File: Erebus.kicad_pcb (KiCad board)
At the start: 2 copper layers, 7 parts, among them U1 STM32F303CBTx, U2 74HC4067, U3 74HC4067, U4 74HC4067, U5 74HC4067, U6 74HC4067, U7 74HC4067

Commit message: Added All the Keyswitches Required
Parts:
- added C1: 100n, Capacitor_SMD:C_0402_1005Metric, F.Cu at (-203.2, 256.6)
- added C10: 100n, Capacitor_SMD:C_0402_1005Metric, F.Cu at (-153.1, 282.8)
- added C100: 100n, Capacitor_SMD:C_0402_1005Metric, F.Cu at (-128.1, 282.8)
- added C101: 100n, Capacitor_SMD:C_0402_1005Metric, F.Cu at (-27.9, 280.8)
- added C102: 100n, Capacitor_SMD:C_0402_1005Metric, F.Cu at (-27.9, 282.8)
- added C103: 100n, Capacitor_SMD:C_0402_1005Metric, F.Cu at (-178.2, 280.8)
- added C104: 100n, Capacitor_SMD:C_0402_1005Metric, F.Cu at (-178.2, 282.8)
- added C105: 100n, Capacitor_SMD:C_0402_1005Metric, F.Cu at (-143.1, 192.1)
- added C106: 100n, Capacitor_SMD:C_0402_1005Metric, F.Cu at (-143.1, 194.1)
- added C107: 100n, Capacitor_SMD:C_0402_1005Metric, F.Cu at (-178.2, 256.6)
- added C108: 100n, Capacitor_SMD:C_0402_1005Metric, F.Cu at (-178.2, 258.6)
- added C109: 100n, Capacitor_SMD:C_0402_1005Metric, F.Cu at (-42.9, 216.3)
- added C11: 100n, Capacitor_SMD:C_0402_1005Metric, F.Cu at (-143.1, 216.3)
- added C110: 100n, Capacitor_SMD:C_0402_1005Metric, F.Cu at (-42.9, 218.3)
- added C111: 100n, Capacitor_SMD:C_0402_1005Metric, F.Cu at (-78.0, 280.8)
- added C112: 100n, Capacitor_SMD:C_0402_1005Metric, F.Cu at (-78.0, 282.8)
- added C113: 100n, Capacitor_SMD:C_0402_1005Metric, F.Cu at (-178.2, 329.1)
- added C114: 100n, Capacitor_SMD:C_0402_1005Metric, F.Cu at (-178.2, 331.1)
- added C115: 100n, Capacitor_SMD:C_0402_1005Metric, F.Cu at (-53.0, 377.4)
- added C116: 100n, Capacitor_SMD:C_0402_1005Metric, F.Cu at (-53.0, 379.4)
- added C117: 100n, Capacitor_SMD:C_0402_1005Metric, F.Cu at (-118.0, 192.1)
- added C118: 100n, Capacitor_SMD:C_0402_1005Metric, F.Cu at (-118.0, 194.1)
- added C119: 100n, Capacitor_SMD:C_0402_1005Metric, F.Cu at (-53.0, 304.9)
- added C12: 100n, Capacitor_SMD:C_0402_1005Metric, F.Cu at (-143.1, 218.3)
- added C120: 100n, Capacitor_SMD:C_0402_1005Metric, F.Cu at (-53.0, 306.9)
- added C121: 100n, Capacitor_SMD:C_0402_1005Metric, F.Cu at (-2.90, 401.6)
- added C122: 100n, Capacitor_SMD:C_0402_1005Metric, F.Cu at (-2.90, 403.6)
- added C123: 100n, Capacitor_SMD:C_0402_1005Metric, F.Cu at (-103.1, 329.1)
- added C124: 100n, Capacitor_SMD:C_0402_1005Metric, F.Cu at (-103.1, 331.1)
- added C125: 100n, Capacitor_SMD:C_0402_1005Metric, F.Cu at (-228.3, 377.4)
- added C126: 100n, Capacitor_SMD:C_0402_1005Metric, F.Cu at (-228.3, 379.4)
- added C127: 100n, Capacitor_SMD:C_0402_1005Metric, F.Cu at (-27.9, 377.4)
- added C128: 100n, Capacitor_SMD:C_0402_1005Metric, F.Cu at (-27.9, 379.4)
- added C129: 100n, Capacitor_SMD:C_0402_1005Metric, F.Cu at (-128.1, 256.6)
- added C13: 100n, Capacitor_SMD:C_0402_1005Metric, F.Cu at (-103.1, 377.4)
- added C130: 100n, Capacitor_SMD:C_0402_1005Metric, F.Cu at (-128.1, 258.6)
- added C131: 100n, Capacitor_SMD:C_0402_1005Metric, F.Cu at (-153.1, 329.1)
- added C132: 100n, Capacitor_SMD:C_0402_1005Metric, F.Cu at (-153.1, 331.1)
- added C133: 100n, Capacitor_SMD:C_0402_1005Metric, F.Cu at (-203.2, 280.8)
- added C134: 100n, Capacitor_SMD:C_0402_1005Metric, F.Cu at (-203.2, 282.8)
- added C135: 100n, Capacitor_SMD:C_0402_1005Metric, F.Cu at (-128.1, 304.9)
- added C136: 100n, Capacitor_SMD:C_0402_1005Metric, F.Cu at (-128.1, 306.9)
- added C137: 100n, Capacitor_SMD:C_0402_1005Metric, F.Cu at (-228.3, 353.3)
- added C138: 100n, Capacitor_SMD:C_0402_1005Metric, F.Cu at (-228.3, 355.2)
- added C139: 100n, Capacitor_SMD:C_0402_1005Metric, F.Cu at (-27.9, 329.1)
- added C14: 100n, Capacitor_SMD:C_0402_1005Metric, F.Cu at (-103.1, 379.4)
- added C140: 100n, Capacitor_SMD:C_0402_1005Metric, F.Cu at (-27.9, 331.1)
- added C141: 100n, Capacitor_SMD:C_0402_1005Metric, F.Cu at (-2.90, 256.6)
- added C142: 100n, Capacitor_SMD:C_0402_1005Metric, F.Cu at (-2.90, 258.6)
- added C143: 100n, Capacitor_SMD:C_0402_1005Metric, F.Cu at (-203.2, 353.3)
- added C144: 100n, Capacitor_SMD:C_0402_1005Metric, F.Cu at (-203.2, 355.2)
- added C145: 100n, Capacitor_SMD:C_0402_1005Metric, F.Cu at (-17.9, 192.1)
- added C146: 100n, Capacitor_SMD:C_0402_1005Metric, F.Cu at (-17.9, 194.1)
- added C147: 100n, Capacitor_SMD:C_0402_1005Metric, F.Cu at (-228.3, 280.8)
- added C148: 100n, Capacitor_SMD:C_0402_1005Metric, F.Cu at (-228.3, 282.8)
- added C149: 100n, Capacitor_SMD:C_0402_1005Metric, F.Cu at (-178.2, 377.4)
- added C15: 100n, Capacitor_SMD:C_0402_1005Metric, F.Cu at (-27.9, 304.9)
- added C150: 100n, Capacitor_SMD:C_0402_1005Metric, F.Cu at (-178.2, 379.4)
- added C151: 100n, Capacitor_SMD:C_0402_1005Metric, F.Cu at (-203.2, 377.4)
- added C152: 100n, Capacitor_SMD:C_0402_1005Metric, F.Cu at (-203.2, 379.4)
- added C153: 100n, Capacitor_SMD:C_0402_1005Metric, F.Cu at (-53.0, 280.8)
- added C154: 100n, Capacitor_SMD:C_0402_1005Metric, F.Cu at (-53.0, 282.8)
- added C155: 100n, Capacitor_SMD:C_0402_1005Metric, F.Cu at (-93.0, 216.3)
- added C156: 100n, Capacitor_SMD:C_0402_1005Metric, F.Cu at (-93.0, 218.3)
- added C157: 100n, Capacitor_SMD:C_0402_1005Metric, F.Cu at (-103.1, 304.9)
- added C158: 100n, Capacitor_SMD:C_0402_1005Metric, F.Cu at (-103.1, 306.9)
- added C159: 100n, Capacitor_SMD:C_0402_1005Metric, F.Cu at (-78.0, 329.1)
- added C16: 100n, Capacitor_SMD:C_0402_1005Metric, F.Cu at (-27.9, 306.9)
- added C160: 100n, Capacitor_SMD:C_0402_1005Metric, F.Cu at (-78.0, 331.1)
- added C161: 100n, Capacitor_SMD:C_0402_1005Metric, F.Cu at (-153.1, 304.9)
- added C162: 100n, Capacitor_SMD:C_0402_1005Metric, F.Cu at (-153.1, 306.9)
- added C163: 100n, Capacitor_SMD:C_0402_1005Metric, F.Cu at (-128.1, 401.6)
- added C164: 100n, Capacitor_SMD:C_0402_1005Metric, F.Cu at (-128.1, 403.6)
- added C17: 100n, Capacitor_SMD:C_0402_1005Metric, F.Cu at (-153.1, 401.6)
- added C18: 100n, Capacitor_SMD:C_0402_1005Metric, F.Cu at (-153.1, 403.6)
- added C19: 100n, Capacitor_SMD:C_0402_1005Metric, F.Cu at (-203.2, 304.9)
- added C2: 100n, Capacitor_SMD:C_0402_1005Metric, F.Cu at (-203.2, 258.6)
- added C20: 100n, Capacitor_SMD:C_0402_1005Metric, F.Cu at (-203.2, 306.9)
- added C21: 100n, Capacitor_SMD:C_0402_1005Metric, F.Cu at (-153.1, 353.3)
- added C22: 100n, Capacitor_SMD:C_0402_1005Metric, F.Cu at (-153.1, 355.2)
- added C23: 100n, Capacitor_SMD:C_0402_1005Metric, F.Cu at (-78.0, 353.3)
- added C24: 100n, Capacitor_SMD:C_0402_1005Metric, F.Cu at (-78.0, 355.2)
- added C25: 100n, Capacitor_SMD:C_0402_1005Metric, F.Cu at (-42.9, 192.1)
- added C26: 100n, Capacitor_SMD:C_0402_1005Metric, F.Cu at (-42.9, 194.1)
- added C27: 100n, Capacitor_SMD:C_0402_1005Metric, F.Cu at (-78.0, 401.6)
- added C28: 100n, Capacitor_SMD:C_0402_1005Metric, F.Cu at (-78.0, 403.6)
- added C29: 100n, Capacitor_SMD:C_0402_1005Metric, F.Cu at (-78.0, 377.4)
- added C3: 100n, Capacitor_SMD:C_0402_1005Metric, F.Cu at (-2.90, 304.9)
- added C30: 100n, Capacitor_SMD:C_0402_1005Metric, F.Cu at (-78.0, 379.4)
- added C31: 100n, Capacitor_SMD:C_0402_1005Metric, F.Cu at (-2.90, 353.3)
- added C32: 100n, Capacitor_SMD:C_0402_1005Metric, F.Cu at (-2.90, 355.2)
- added C33: 100n, Capacitor_SMD:C_0402_1005Metric, F.Cu at (-103.1, 401.6)
- added C34: 100n, Capacitor_SMD:C_0402_1005Metric, F.Cu at (-103.1, 403.6)
- added C35: 100n, Capacitor_SMD:C_0402_1005Metric, F.Cu at (-2.90, 329.1)
- added C36: 100n, Capacitor_SMD:C_0402_1005Metric, F.Cu at (-2.90, 331.1)
- added C37: 100n, Capacitor_SMD:C_0402_1005Metric, F.Cu at (-2.90, 377.4)
- added C38: 100n, Capacitor_SMD:C_0402_1005Metric, F.Cu at (-2.90, 379.4)
- added C39: 100n, Capacitor_SMD:C_0402_1005Metric, F.Cu at (-27.9, 353.3)
- added C4: 100n, Capacitor_SMD:C_0402_1005Metric, F.Cu at (-2.90, 306.9)
- added C40: 100n, Capacitor_SMD:C_0402_1005Metric, F.Cu at (-27.9, 355.2)
- added C41: 100n, Capacitor_SMD:C_0402_1005Metric, F.Cu at (-128.1, 353.3)
- added C42: 100n, Capacitor_SMD:C_0402_1005Metric, F.Cu at (-128.1, 355.2)
- added C43: 100n, Capacitor_SMD:C_0402_1005Metric, F.Cu at (-103.1, 353.3)
- added C44: 100n, Capacitor_SMD:C_0402_1005Metric, F.Cu at (-103.1, 355.2)
- added C45: 100n, Capacitor_SMD:C_0402_1005Metric, F.Cu at (-118.0, 216.3)
- added C46: 100n, Capacitor_SMD:C_0402_1005Metric, F.Cu at (-118.0, 218.3)
- added C47: 100n, Capacitor_SMD:C_0402_1005Metric, F.Cu at (-153.1, 377.4)
- added C48: 100n, Capacitor_SMD:C_0402_1005Metric, F.Cu at (-153.1, 379.4)
- added C49: 100n, Capacitor_SMD:C_0402_1005Metric, F.Cu at (-103.1, 280.8)
- added C5: 100n, Capacitor_SMD:C_0402_1005Metric, F.Cu at (-103.1, 256.6)
- added C50: 100n, Capacitor_SMD:C_0402_1005Metric, F.Cu at (-103.1, 282.8)
- added C51: 100n, Capacitor_SMD:C_0402_1005Metric, F.Cu at (-128.1, 377.4)
- added C52: 100n, Capacitor_SMD:C_0402_1005Metric, F.Cu at (-128.1, 379.4)
- added C53: 100n, Capacitor_SMD:C_0402_1005Metric, F.Cu at (-27.9, 256.6)
- added C54: 100n, Capacitor_SMD:C_0402_1005Metric, F.Cu at (-27.9, 258.6)
- added C55: 100n, Capacitor_SMD:C_0402_1005Metric, F.Cu at (-78.0, 304.9)
- added C56: 100n, Capacitor_SMD:C_0402_1005Metric, F.Cu at (-78.0, 306.9)
- added C57: 100n, Capacitor_SMD:C_0402_1005Metric, F.Cu at (-203.2, 329.1)
- added C58: 100n, Capacitor_SMD:C_0402_1005Metric, F.Cu at (-203.2, 331.1)
- added C59: 100n, Capacitor_SMD:C_0402_1005Metric, F.Cu at (-53.0, 401.6)
- added C6: 100n, Capacitor_SMD:C_0402_1005Metric, F.Cu at (-103.1, 258.6)
- added C60: 100n, Capacitor_SMD:C_0402_1005Metric, F.Cu at (-53.0, 403.6)
- added C61: 100n, Capacitor_SMD:C_0402_1005Metric, F.Cu at (-2.90, 280.8)
- added C62: 100n, Capacitor_SMD:C_0402_1005Metric, F.Cu at (-2.90, 282.8)
- added C63: 100n, Capacitor_SMD:C_0402_1005Metric, F.Cu at (-178.2, 353.3)
- added C64: 100n, Capacitor_SMD:C_0402_1005Metric, F.Cu at (-178.2, 355.2)
- added C65: 100n, Capacitor_SMD:C_0402_1005Metric, F.Cu at (-53.0, 329.1)
- added C66: 100n, Capacitor_SMD:C_0402_1005Metric, F.Cu at (-53.0, 331.1)
- added C67: 100n, Capacitor_SMD:C_0402_1005Metric, F.Cu at (-78.0, 256.6)
- added C68: 100n, Capacitor_SMD:C_0402_1005Metric, F.Cu at (-78.0, 258.6)
- added C69: 100n, Capacitor_SMD:C_0402_1005Metric, F.Cu at (-203.2, 401.6)
- added C7: 100n, Capacitor_SMD:C_0402_1005Metric, F.Cu at (-153.1, 256.6)
- added C70: 100n, Capacitor_SMD:C_0402_1005Metric, F.Cu at (-203.2, 403.6)
- added C71: 100n, Capacitor_SMD:C_0402_1005Metric, F.Cu at (-53.0, 256.6)
- added C72: 100n, Capacitor_SMD:C_0402_1005Metric, F.Cu at (-53.0, 258.6)
- added C73: 100n, Capacitor_SMD:C_0402_1005Metric, F.Cu at (-228.3, 329.1)
- added C74: 100n, Capacitor_SMD:C_0402_1005Metric, F.Cu at (-228.3, 331.1)
- added C75: 100n, Capacitor_SMD:C_0402_1005Metric, F.Cu at (-228.3, 304.9)
- added C76: 100n, Capacitor_SMD:C_0402_1005Metric, F.Cu at (-228.3, 306.9)
- added C77: 100n, Capacitor_SMD:C_0402_1005Metric, F.Cu at (-67.9, 216.3)
- added C78: 100n, Capacitor_SMD:C_0402_1005Metric, F.Cu at (-67.9, 218.3)
- added C79: 100n, Capacitor_SMD:C_0402_1005Metric, F.Cu at (-178.2, 401.6)
- added C8: 100n, Capacitor_SMD:C_0402_1005Metric, F.Cu at (-153.1, 258.6)
- added C80: 100n, Capacitor_SMD:C_0402_1005Metric, F.Cu at (-178.2, 403.6)
- added C81: 100n, Capacitor_SMD:C_0402_1005Metric, F.Cu at (-27.9, 401.6)
- added C82: 100n, Capacitor_SMD:C_0402_1005Metric, F.Cu at (-27.9, 403.6)
- added C83: 100n, Capacitor_SMD:C_0402_1005Metric, F.Cu at (-228.3, 256.6)
- added C84: 100n, Capacitor_SMD:C_0402_1005Metric, F.Cu at (-228.3, 258.6)
- added C85: 100n, Capacitor_SMD:C_0402_1005Metric, F.Cu at (-53.0, 353.3)
- added C86: 100n, Capacitor_SMD:C_0402_1005Metric, F.Cu at (-53.0, 355.2)
- added C87: 100n, Capacitor_SMD:C_0402_1005Metric, F.Cu at (-17.9, 216.3)
- added C88: 100n, Capacitor_SMD:C_0402_1005Metric, F.Cu at (-17.9, 218.3)
- added C89: 100n, Capacitor_SMD:C_0402_1005Metric, F.Cu at (-128.1, 329.1)
- added C9: 100n, Capacitor_SMD:C_0402_1005Metric, F.Cu at (-153.1, 280.8)
- added C90: 100n, Capacitor_SMD:C_0402_1005Metric, F.Cu at (-128.1, 331.1)
- added C91: 100n, Capacitor_SMD:C_0402_1005Metric, F.Cu at (-93.0, 192.1)
- added C92: 100n, Capacitor_SMD:C_0402_1005Metric, F.Cu at (-93.0, 194.1)
- added C93: 100n, Capacitor_SMD:C_0402_1005Metric, F.Cu at (-228.3, 401.6)
- added C94: 100n, Capacitor_SMD:C_0402_1005Metric, F.Cu at (-228.3, 403.6)
- added C95: 100n, Capacitor_SMD:C_0402_1005Metric, F.Cu at (-178.2, 304.9)
- added C96: 100n, Capacitor_SMD:C_0402_1005Metric, F.Cu at (-178.2, 306.9)
- added C97: 100n, Capacitor_SMD:C_0402_1005Metric, F.Cu at (-67.9, 192.1)
- added C98: 100n, Capacitor_SMD:C_0402_1005Metric, F.Cu at (-67.9, 194.1)
- added C99: 100n, Capacitor_SMD:C_0402_1005Metric, F.Cu at (-128.1, 280.8)
- added R1: 10k, Resistor_SMD:R_0402_1005Metric, F.Cu at (-223.4, 276.8)
- added R10: 10k, Resistor_SMD:R_0402_1005Metric, F.Cu at (-223.4, 325.1)
- added R11: 10k, Resistor_SMD:R_0402_1005Metric, F.Cu at (-173.3, 373.4)
- added R12: 10k, Resistor_SMD:R_0402_1005Metric, F.Cu at (-98.2, 373.4)
- added R13: 10k, Resistor_SMD:R_0402_1005Metric, F.Cu at (-63.0, 212.3)
- added R14: 10k, Resistor_SMD:R_0402_1005Metric, F.Cu at (-98.2, 421.8)
- added R15: 10k, Resistor_SMD:R_0402_1005Metric, F.Cu at (-98.2, 397.6)
- added R16: 10k, Resistor_SMD:R_0402_1005Metric, F.Cu at (-23.1, 373.4)
- added R17: 10k, Resistor_SMD:R_0402_1005Metric, F.Cu at (-123.2, 421.8)
- added R18: 10k, Resistor_SMD:R_0402_1005Metric, F.Cu at (-23.1, 349.3)
- added R19: 10k, Resistor_SMD:R_0402_1005Metric, F.Cu at (-23.1, 397.6)
- added R2: 10k, Resistor_SMD:R_0402_1005Metric, F.Cu at (-23.1, 325.1)
- added R20: 10k, Resistor_SMD:R_0402_1005Metric, F.Cu at (-48.1, 373.4)
- added R21: 10k, Resistor_SMD:R_0402_1005Metric, F.Cu at (-148.2, 373.4)
- added R22: 10k, Resistor_SMD:R_0402_1005Metric, F.Cu at (-123.2, 373.4)
- added R23: 10k, Resistor_SMD:R_0402_1005Metric, F.Cu at (-138.2, 236.5)
- added R24: 10k, Resistor_SMD:R_0402_1005Metric, F.Cu at (-173.3, 397.6)
- added R25: 10k, Resistor_SMD:R_0402_1005Metric, F.Cu at (-123.2, 301.0)
- added R26: 10k, Resistor_SMD:R_0402_1005Metric, F.Cu at (-148.2, 397.6)
- added R27: 10k, Resistor_SMD:R_0402_1005Metric, F.Cu at (-48.1, 276.8)
- added R28: 10k, Resistor_SMD:R_0402_1005Metric, F.Cu at (-98.2, 325.1)
- added R29: 10k, Resistor_SMD:R_0402_1005Metric, F.Cu at (-223.4, 349.3)
- added R3: 10k, Resistor_SMD:R_0402_1005Metric, F.Cu at (-123.2, 276.8)
- added R30: 10k, Resistor_SMD:R_0402_1005Metric, F.Cu at (-73.1, 421.8)
- added R31: 10k, Resistor_SMD:R_0402_1005Metric, F.Cu at (-23.1, 301.0)
- added R32: 10k, Resistor_SMD:R_0402_1005Metric, F.Cu at (-198.3, 373.4)
- added R33: 10k, Resistor_SMD:R_0402_1005Metric, F.Cu at (-73.1, 349.3)
- added R34: 10k, Resistor_SMD:R_0402_1005Metric, F.Cu at (-98.2, 276.8)
- added R35: 10k, Resistor_SMD:R_0402_1005Metric, F.Cu at (-223.4, 421.8)
- added R36: 10k, Resistor_SMD:R_0402_1005Metric, F.Cu at (-73.1, 276.8)
- added R37: 10k, Resistor_SMD:R_0402_1005Metric, F.Cu at (-248.4, 349.3)
- added R38: 10k, Resistor_SMD:R_0402_1005Metric, F.Cu at (-248.4, 325.1)
- added R39: 10k, Resistor_SMD:R_0402_1005Metric, F.Cu at (-88.1, 236.5)
- added R4: 10k, Resistor_SMD:R_0402_1005Metric, F.Cu at (-173.3, 276.8)
- added R40: 10k, Resistor_SMD:R_0402_1005Metric, F.Cu at (-198.3, 421.8)
- added R41: 10k, Resistor_SMD:R_0402_1005Metric, F.Cu at (-48.1, 421.8)
- added R42: 10k, Resistor_SMD:R_0402_1005Metric, F.Cu at (-248.4, 276.8)
- added R43: 10k, Resistor_SMD:R_0402_1005Metric, F.Cu at (-73.1, 373.4)
- added R44: 10k, Resistor_SMD:R_0402_1005Metric, F.Cu at (-38.0, 236.5)
- added R45: 10k, Resistor_SMD:R_0402_1005Metric, F.Cu at (-148.2, 349.3)
- added R46: 10k, Resistor_SMD:R_0402_1005Metric, F.Cu at (-113.1, 212.3)
- added R47: 10k, Resistor_SMD:R_0402_1005Metric, F.Cu at (-248.4, 421.8)
- added R48: 10k, Resistor_SMD:R_0402_1005Metric, F.Cu at (-198.3, 325.1)
- added R49: 10k, Resistor_SMD:R_0402_1005Metric, F.Cu at (-88.1, 212.3)
- added R5: 10k, Resistor_SMD:R_0402_1005Metric, F.Cu at (-173.3, 301.0)
- added R50: 10k, Resistor_SMD:R_0402_1005Metric, F.Cu at (-148.2, 301.0)
- added R51: 10k, Resistor_SMD:R_0402_1005Metric, F.Cu at (-48.1, 301.0)
- added R52: 10k, Resistor_SMD:R_0402_1005Metric, F.Cu at (-198.3, 301.0)
- added R53: 10k, Resistor_SMD:R_0402_1005Metric, F.Cu at (-163.2, 212.3)
- added R54: 10k, Resistor_SMD:R_0402_1005Metric, F.Cu at (-198.3, 276.8)
- added R55: 10k, Resistor_SMD:R_0402_1005Metric, F.Cu at (-63.0, 236.5)
- added R56: 10k, Resistor_SMD:R_0402_1005Metric, F.Cu at (-98.2, 301.0)
- added R57: 10k, Resistor_SMD:R_0402_1005Metric, F.Cu at (-198.3, 349.3)
- added R58: 10k, Resistor_SMD:R_0402_1005Metric, F.Cu at (-73.1, 397.6)
- added R59: 10k, Resistor_SMD:R_0402_1005Metric, F.Cu at (-138.2, 212.3)
- added R6: 10k, Resistor_SMD:R_0402_1005Metric, F.Cu at (-163.2, 236.5)
- added R60: 10k, Resistor_SMD:R_0402_1005Metric, F.Cu at (-73.1, 325.1)
- added R61: 10k, Resistor_SMD:R_0402_1005Metric, F.Cu at (-23.1, 421.8)
- added R62: 10k, Resistor_SMD:R_0402_1005Metric, F.Cu at (-123.2, 349.3)
- added R63: 10k, Resistor_SMD:R_0402_1005Metric, F.Cu at (-248.4, 397.6)
- added R64: 10k, Resistor_SMD:R_0402_1005Metric, F.Cu at (-48.1, 397.6)
- added R65: 10k, Resistor_SMD:R_0402_1005Metric, F.Cu at (-148.2, 276.8)
- added R66: 10k, Resistor_SMD:R_0402_1005Metric, F.Cu at (-173.3, 349.3)
- added R67: 10k, Resistor_SMD:R_0402_1005Metric, F.Cu at (-223.4, 301.0)
- added R68: 10k, Resistor_SMD:R_0402_1005Metric, F.Cu at (-148.2, 325.1)
- added R69: 10k, Resistor_SMD:R_0402_1005Metric, F.Cu at (-248.4, 373.4)
- added R7: 10k, Resistor_SMD:R_0402_1005Metric, F.Cu at (-123.2, 397.6)
- added R70: 10k, Resistor_SMD:R_0402_1005Metric, F.Cu at (-48.1, 349.3)
- added R71: 10k, Resistor_SMD:R_0402_1005Metric, F.Cu at (-23.1, 276.8)
- added R72: 10k, Resistor_SMD:R_0402_1005Metric, F.Cu at (-223.4, 373.4)
- added R73: 10k, Resistor_SMD:R_0402_1005Metric, F.Cu at (-38.0, 212.3)
- added R74: 10k, Resistor_SMD:R_0402_1005Metric, F.Cu at (-248.4, 301.0)
- added R75: 10k, Resistor_SMD:R_0402_1005Metric, F.Cu at (-198.3, 397.6)
- added R76: 10k, Resistor_SMD:R_0402_1005Metric, F.Cu at (-223.4, 397.6)
- added R77: 10k, Resistor_SMD:R_0402_1005Metric, F.Cu at (-73.1, 301.0)
- added R78: 10k, Resistor_SMD:R_0402_1005Metric, F.Cu at (-113.1, 236.5)
- added R79: 10k, Resistor_SMD:R_0402_1005Metric, F.Cu at (-123.2, 325.1)
- added R8: 10k, Resistor_SMD:R_0402_1005Metric, F.Cu at (-48.1, 325.1)
- added R80: 10k, Resistor_SMD:R_0402_1005Metric, F.Cu at (-98.2, 349.3)
- added R81: 10k, Resistor_SMD:R_0402_1005Metric, F.Cu at (-173.3, 325.1)
- added R82: 10k, Resistor_SMD:R_0402_1005Metric, F.Cu at (-148.2, 421.8)
- added R9: 10k, Resistor_SMD:R_0402_1005Metric, F.Cu at (-173.3, 421.8)
- renumbered U5 to U3, U3 to U4, U6 to U5, U4 to U6
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
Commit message: Setup Base Layout
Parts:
- removed R82: 10k, Resistor_SMD:R_0402_1005Metric
- removed S1, S4: MX_stab, PCM_marbastlib-mx:STAB_MX_P_2.25u
- removed S2: MX_stab, PCM_marbastlib-mx:STAB_MX_P_2u
- removed S3: MX_stab, PCM_marbastlib-mx:STAB_MX_P_2.75u
- removed U10, U11, U12, U13, U14, U15, U16, U17, U18, U19, U20, U21, U22, U23, U24, U25, U26, U27, U28, U29, U30, U31, U32, U33, U34, U35, U36, U37, U38, U39, U40, U41, U42, U43, U44, U45, U46, U47, U48, U49, U50, U51, U52, U53, U54, U55, U56, U57, U58, U59, U60, U61, U62, U63, U64, U65, U66, U67, U68, U69, U70, U71, U72, U73, U74, U75, U76, U77, U78, U79, U8, U80, U81, U82, U83, U84, U85, U86, U87, U88, U89, U9: SLSS49E-3, Erebus:SLSS49E-3 with MX holes
- added C165: 100n, Capacitor_SMD:C_0402_1005Metric, B.Cu at (472.6, 188.1)
- added C166: 100n, Capacitor_SMD:C_0402_1005Metric, B.Cu at (478.2, 187.0)
- added C167: 100n, Capacitor_SMD:C_0402_1005Metric, B.Cu at (299.5, 182.5)
- added C168: 100n, Capacitor_SMD:C_0402_1005Metric, B.Cu at (304.8, 180.3)
- added ENCODER1: EC11E, PCM_marbastlib-various:ROT_Alps_EC11E-Switch, F.Cu at (434.9, 83.3)
- added JP1: Jumper_2_Open, Connector_PinHeader_2.54mm:PinHeader_1x02_P2.54mm_Vertical, F.Cu at (282.5, 161.3)
- added JP2: Jumper_2_Open, Connector_PinHeader_2.54mm:PinHeader_1x02_P2.54mm_Vertical, F.Cu at (287.2, 161.3)
- added S28: MX_stab, PCM_marbastlib-mx:STAB_MX_P_2u, F.Cu at (432.1, 107.5)
- added S57: MX_stab, PCM_marbastlib-mx:STAB_MX_P_2.25u, F.Cu at (439.2, 145.6)
- added S59: MX_stab, PCM_marbastlib-mx:STAB_MX_P_2.25u, F.Cu at (154.4, 164.7)
- added S75: MX_stab, PCM_marbastlib-mx:STAB_MX_P_2u, F.Cu at (241.9, 193.0)
- added S77: MX_stab, PCM_marbastlib-mx:STAB_MX_P_2.75u, F.Cu at (331.4, 195.6)
- added SW1: SLSS49E-3, Erebus:SLSS49E-3 with MX holes, B.Cu at (146.3, 83.7)
- added SW10: SLSS49E-3, Erebus:SLSS49E-3 with MX holes, B.Cu at (350.2, 89.4)
- added SW11: SLSS49E-3, Erebus:SLSS49E-3 with MX holes, B.Cu at (368.9, 85.4)
- added SW12: SLSS49E-3, Erebus:SLSS49E-3 with MX holes, B.Cu at (390.1, 82.8)
- added SW13: SLSS49E-3, Erebus:SLSS49E-3 with MX holes, B.Cu at (409.2, 82.8)
- added SW14: SLSS49E-3, Erebus:SLSS49E-3 with MX holes, B.Cu at (460.6, 83.7)
- added SW15: SLSS49E-3, Erebus:SLSS49E-3 with MX holes, B.Cu at (156.8, 107.5)
- added SW16: SLSS49E-3, Erebus:SLSS49E-3 with MX holes, B.Cu at (175.8, 107.5)
- added SW17: SLSS49E-3, Erebus:SLSS49E-3 with MX holes, B.Cu at (194.9, 104.7)
- added SW18: SLSS49E-3, Erebus:SLSS49E-3 with MX holes, B.Cu at (215.8, 109.6)
- added SW19: SLSS49E-3, Erebus:SLSS49E-3 with MX holes, B.Cu at (234.4, 113.5)
- added SW2: SLSS49E-3, Erebus:SLSS49E-3 with MX holes, B.Cu at (171.1, 82.8)
- added SW20: SLSS49E-3, Erebus:SLSS49E-3 with MX holes, B.Cu at (253.1, 117.5)
- added SW21: SLSS49E-3, Erebus:SLSS49E-3 with MX holes, B.Cu at (271.7, 121.5)
- added SW22: SLSS49E-3, Erebus:SLSS49E-3 with MX holes, B.Cu at (308.6, 122.6)
- added SW23: SLSS49E-3, Erebus:SLSS49E-3 with MX holes, B.Cu at (327.2, 118.6)
- added SW24: SLSS49E-3, Erebus:SLSS49E-3 with MX holes, B.Cu at (345.9, 114.7)
- added SW25: SLSS49E-3, Erebus:SLSS49E-3 with MX holes, B.Cu at (364.5, 110.7)
- added SW26: SLSS49E-3, Erebus:SLSS49E-3 with MX holes, B.Cu at (384.4, 104.7)
- added SW27: SLSS49E-3, Erebus:SLSS49E-3 with MX holes, B.Cu at (403.5, 107.5)
- added SW28: SLSS49E-3, Erebus:SLSS49E-3 with MX holes, B.Cu at (432.1, 107.5)
- added SW29: SLSS49E-3, Erebus:SLSS49E-3 with MX holes, B.Cu at (465.4, 102.8)
- added SW3: SLSS49E-3, Erebus:SLSS49E-3 with MX holes, B.Cu at (190.1, 82.8)
- added SW30: SLSS49E-3, Erebus:SLSS49E-3 with MX holes, B.Cu at (156.8, 126.6)
- added SW31: SLSS49E-3, Erebus:SLSS49E-3 with MX holes, B.Cu at (180.6, 126.6)
- added SW32: SLSS49E-3, Erebus:SLSS49E-3 with MX holes, B.Cu at (202.5, 126.2)
- added SW33: SLSS49E-3, Erebus:SLSS49E-3 with MX holes, B.Cu at (221.2, 130.2)
- added SW34: SLSS49E-3, Erebus:SLSS49E-3 with MX holes, B.Cu at (239.8, 134.1)
- added SW35: SLSS49E-3, Erebus:SLSS49E-3 with MX holes, B.Cu at (258.4, 138.1)
- added SW36: SLSS49E-3, Erebus:SLSS49E-3 with MX holes, B.Cu at (303.3, 143.2)
- added SW37: SLSS49E-3, Erebus:SLSS49E-3 with MX holes, B.Cu at (321.9, 139.2)
- added SW38: SLSS49E-3, Erebus:SLSS49E-3 with MX holes, B.Cu at (340.5, 135.3)
- added SW39: SLSS49E-3, Erebus:SLSS49E-3 with MX holes, B.Cu at (359.2, 131.3)
- added SW4: SLSS49E-3, Erebus:SLSS49E-3 with MX holes, B.Cu at (211.4, 84.3)
- added SW40: SLSS49E-3, Erebus:SLSS49E-3 with MX holes, B.Cu at (377.8, 127.4)
- added SW41: SLSS49E-3, Erebus:SLSS49E-3 with MX holes, B.Cu at (398.7, 126.6)
- added SW42: SLSS49E-3, Erebus:SLSS49E-3 with MX holes, B.Cu at (417.8, 126.6)
- added SW43: SLSS49E-3, Erebus:SLSS49E-3 with MX holes, B.Cu at (441.6, 126.6)
- added SW44: SLSS49E-3, Erebus:SLSS49E-3 with MX holes, B.Cu at (470.2, 121.8)
- added SW45: SLSS49E-3, Erebus:SLSS49E-3 with MX holes, B.Cu at (149.6, 145.6)
- added SW46: SLSS49E-3, Erebus:SLSS49E-3 with MX holes, B.Cu at (180.6, 145.6)
- added SW47: SLSS49E-3, Erebus:SLSS49E-3 with MX holes, B.Cu at (203.2, 145.8)
- added SW48: SLSS49E-3, Erebus:SLSS49E-3 with MX holes, B.Cu at (221.9, 149.8)
- added SW49: SLSS49E-3, Erebus:SLSS49E-3 with MX holes, B.Cu at (240.5, 153.8)
- added SW5: SLSS49E-3, Erebus:SLSS49E-3 with MX holes, B.Cu at (230.1, 88.3)
- added SW50: SLSS49E-3, Erebus:SLSS49E-3 with MX holes, B.Cu at (259.1, 157.7)
- added SW51: SLSS49E-3, Erebus:SLSS49E-3 with MX holes, B.Cu at (311.9, 160.9)
- added SW52: SLSS49E-3, Erebus:SLSS49E-3 with MX holes, B.Cu at (330.5, 156.9)
- added SW53: SLSS49E-3, Erebus:SLSS49E-3 with MX holes, B.Cu at (349.1, 152.9)
- added SW54: SLSS49E-3, Erebus:SLSS49E-3 with MX holes, B.Cu at (367.8, 149.0)
- added SW55: SLSS49E-3, Erebus:SLSS49E-3 with MX holes, B.Cu at (389.2, 145.6)
- added SW56: SLSS49E-3, Erebus:SLSS49E-3 with MX holes, B.Cu at (408.2, 145.6)
- added SW57: SLSS49E-3, Erebus:SLSS49E-3 with MX holes, B.Cu at (439.2, 145.6)
- added SW58: SLSS49E-3, Erebus:SLSS49E-3 with MX holes, B.Cu at (474.9, 140.9)
- added SW59: SLSS49E-3, Erebus:SLSS49E-3 with MX holes, B.Cu at (154.4, 164.7)
- added SW6: SLSS49E-3, Erebus:SLSS49E-3 with MX holes, B.Cu at (253.4, 93.2)
- added SW60: SLSS49E-3, Erebus:SLSS49E-3 with MX holes, B.Cu at (185.4, 164.7)
- added SW61: SLSS49E-3, Erebus:SLSS49E-3 with MX holes, B.Cu at (208.6, 166.5)
- added SW62: SLSS49E-3, Erebus:SLSS49E-3 with MX holes, B.Cu at (227.2, 170.4)
- added SW63: SLSS49E-3, Erebus:SLSS49E-3 with MX holes, B.Cu at (245.9, 174.4)
- added SW64: SLSS49E-3, Erebus:SLSS49E-3 with MX holes, B.Cu at (264.5, 178.3)
- added SW65: SLSS49E-3, Erebus:SLSS49E-3 with MX holes, B.Cu at (301.9, 182.5)
- added SW66: SLSS49E-3, Erebus:SLSS49E-3 with MX holes, B.Cu at (320.5, 178.5)
- added SW67: SLSS49E-3, Erebus:SLSS49E-3 with MX holes, B.Cu at (339.1, 174.5)
- added SW68: SLSS49E-3, Erebus:SLSS49E-3 with MX holes, B.Cu at (357.8, 170.6)
- added SW69: SLSS49E-3, Erebus:SLSS49E-3 with MX holes, B.Cu at (376.4, 166.6)
- added SW7: SLSS49E-3, Erebus:SLSS49E-3 with MX holes, B.Cu at (272.0, 97.2)
- added SW70: SLSS49E-3, Erebus:SLSS49E-3 with MX holes, B.Cu at (398.7, 164.7)
- added SW71: SLSS49E-3, Erebus:SLSS49E-3 with MX holes, B.Cu at (424.9, 164.7)
- added SW72: SLSS49E-3, Erebus:SLSS49E-3 with MX holes, B.Cu at (455.9, 169.5)
- added SW73: SLSS49E-3, Erebus:SLSS49E-3 with MX holes, B.Cu at (147.3, 183.7)
- added SW74: SLSS49E-3, Erebus:SLSS49E-3 with MX holes, B.Cu at (209.3, 186.1)
- added SW75: SLSS49E-3, Erebus:SLSS49E-3 with MX holes, B.Cu at (241.9, 193.0)
- added SW76: SLSS49E-3, Erebus:SLSS49E-3 with MX holes, B.Cu at (269.8, 199.0)
- added SW77: SLSS49E-3, Erebus:SLSS49E-3 with MX holes, B.Cu at (331.4, 195.6)
- added SW78: SLSS49E-3, Erebus:SLSS49E-3 with MX holes, B.Cu at (371.0, 187.2)
- added SW79: SLSS49E-3, Erebus:SLSS49E-3 with MX holes, B.Cu at (436.8, 188.5)
- added SW8: SLSS49E-3, Erebus:SLSS49E-3 with MX holes, B.Cu at (308.3, 98.3)
- added SW80: SLSS49E-3, Erebus:SLSS49E-3 with MX holes, B.Cu at (455.9, 188.5)
- added SW81: SLSS49E-3, Erebus:SLSS49E-3 with MX holes, B.Cu at (474.9, 188.5)
- added SW9: SLSS49E-3, Erebus:SLSS49E-3 with MX holes, B.Cu at (327.0, 94.4)
- C1, C10, C100, C101, C102, C103, C104, C105, C106, C107, C108, C109, C11, C110, C111, C112, C113, C114, C115, C116, C117, C118, C119, C12, C120, C121, C122, C123, C124, C125, C126, C127, C128, C129, C13, C130, C131, C132, C133, C134, C135, C136, C137, C138, C139, C14, C140, C141, C142, C143, C144, C145, C146, C147, C148, C149, C15, C150, C151, C152, C153, C154, C155, C156, C157, C158, C159, C16, C160, C161, C162, C163, C164, C17, C18, C19, C2, C20, C21, C22, C23, C24, C25, C26, C27, C28, C29, C3, C30, C31, C32, C33, C34, C35, C36, C37, C38, C39, C4, C40, C41, C42, C43, C44, C45, C46, C47, C48, C49, C5, C50, C51, C52, C53, C54, C55, C56, C57, C58, C59, C6, C60, C61, C62, C63, C64, C65, C66, C67, C68, C69, C7, C70, C71, C72, C73, C74, C75, C76, C77, C78, C79, C8, C80, C81, C82, C83, C84, C85, C86, C87, C88, C89, C9, C90, C91, C92, C93, C94, C95, C96, C97, C98, C99, R1, R10, R11, R12, R13, R14, R15, R16, R17, R18, R19, R2, R20, R21, R22, R23, R24, R25, R26, R27, R28, R29, R3, R30, R31, R32, R33, R34, R35, R36, R37, R38, R39, R4, R40, R41, R42, R43, R44, R45, R46, R47, R48, R49, R5, R50, R51, R52, R53, R54, R55, R56, R57, R58, R59, R6, R60, R61, R62, R63, R64, R65, R66, R67, R68, R69, R7, R70, R71, R72, R73, R74, R75, R76, R77, R78, R79, R8, R80, R81, R9, U2, U3, U4, U5, U6, U7: moved to B.Cu
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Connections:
- C1 pad 1: GND -> +3V3
- C1 pad 2: +3V3 -> GND
- C10 pad 1: /multiplexers/keys/KEYS_0_4 -> /multiplexers/keys/KEYS_0_1
- C100 pad 1: /multiplexers/keys/KEYS_3_3 -> /multiplexers/keys/KEYS_3_2
- C102 pad 1: /multiplexers/keys/KEYS_3_4 -> /multiplexers/keys/KEYS_3_3
- C104 pad 1: /multiplexers/keys/KEYS_3_5 -> /multiplexers/keys/KEYS_3_4
- C106 pad 1: /multiplexers/keys/KEYS_3_6 -> /multiplexers/keys/KEYS_3_5
- C108 pad 1: /multiplexers/keys/KEYS_3_7 -> /multiplexers/keys/KEYS_3_6
- C110 pad 1: /multiplexers/keys/KEYS_3_8 -> /multiplexers/keys/KEYS_3_7
- C112 pad 1: /multiplexers/keys/KEYS_3_9 -> /multiplexers/keys/KEYS_3_8
- C114 pad 1: /multiplexers/keys/KEYS_3_10 -> /multiplexers/keys/KEYS_3_9
- C116 pad 1: /multiplexers/keys/KEYS_3_11 -> /multiplexers/keys/KEYS_3_10
- C118 pad 1: /multiplexers/keys/KEYS_3_12 -> /multiplexers/keys/KEYS_3_11
- C12 pad 1: /multiplexers/keys/KEYS_0_5 -> /multiplexers/keys/KEYS_0_2
- C120 pad 1: /multiplexers/keys/KEYS_3_13 -> /multiplexers/keys/KEYS_3_12
- C122 pad 1: /multiplexers/keys/KEYS_4_0 -> /multiplexers/keys/KEYS_3_13
- C124 pad 1: /multiplexers/keys/KEYS_4_1 -> /multiplexers/keys/KEYS_4_0
- C126 pad 1: /multiplexers/keys/KEYS_4_2 -> /multiplexers/keys/KEYS_4_1
- C128 pad 1: /multiplexers/keys/KEYS_4_3 -> /multiplexers/keys/KEYS_4_2
- C130 pad 1: /multiplexers/keys/KEYS_4_4 -> /multiplexers/keys/KEYS_4_3
- C132 pad 1: /multiplexers/keys/KEYS_4_5 -> /multiplexers/keys/KEYS_4_4
- C134 pad 1: /multiplexers/keys/KEYS_4_6 -> /multiplexers/keys/KEYS_4_5
- C14 pad 1: /multiplexers/keys/KEYS_0_6 -> /multiplexers/keys/KEYS_0_3
- C148 pad 1: /multiplexers/keys/KEYS_5_0 -> /multiplexers/keys/KEYS_4_13
- C150 pad 1: /multiplexers/keys/KEYS_5_1 -> /multiplexers/keys/KEYS_5_0
- C152 pad 1: /multiplexers/keys/KEYS_5_2 -> /multiplexers/keys/KEYS_5_1
- C154 pad 1: /multiplexers/keys/KEYS_5_3 -> /multiplexers/keys/KEYS_5_2
- C156 pad 1: /multiplexers/keys/KEYS_5_4 -> /multiplexers/keys/KEYS_5_3
- C158 pad 1: /multiplexers/keys/KEYS_5_5 -> /multiplexers/keys/KEYS_5_4
- C16 pad 1: /multiplexers/keys/KEYS_0_7 -> /multiplexers/keys/KEYS_0_4
- C160 pad 1: /multiplexers/keys/KEYS_5_6 -> /multiplexers/keys/KEYS_5_5
- C162 pad 1: /multiplexers/keys/KEYS_5_7 -> /multiplexers/keys/KEYS_5_6
- C164 pad 1: /multiplexers/keys/KEYS_5_8 -> /multiplexers/keys/KEYS_5_7
- C18 pad 1: /multiplexers/keys/KEYS_0_8 -> /multiplexers/keys/KEYS_0_5
- C2 pad 1: /multiplexers/keys/KEYS_0_0 -> +3V3
- C20 pad 1: /multiplexers/keys/KEYS_0_9 -> /multiplexers/keys/KEYS_0_6
- C22 pad 1: /multiplexers/keys/KEYS_0_10 -> /multiplexers/keys/KEYS_0_7
- C24 pad 1: /multiplexers/keys/KEYS_0_11 -> /multiplexers/keys/KEYS_0_8
- C26 pad 1: /multiplexers/keys/KEYS_0_12 -> /multiplexers/keys/KEYS_0_9
- C28 pad 1: /multiplexers/keys/KEYS_1_0 -> /multiplexers/keys/KEYS_0_10
- C3 pad 1: GND -> +3V3
- C3 pad 2: +3V3 -> GND
- C30 pad 1: /multiplexers/keys/KEYS_0_13 -> /multiplexers/keys/KEYS_0_11
- C32 pad 1: /multiplexers/keys/KEYS_1_1 -> /multiplexers/keys/KEYS_0_12
- C34 pad 1: /multiplexers/keys/KEYS_1_2 -> /multiplexers/keys/KEYS_1_0
- C36 pad 1: /multiplexers/keys/KEYS_1_3 -> /multiplexers/keys/KEYS_0_13
- C38 pad 1: /multiplexers/keys/KEYS_1_4 -> /multiplexers/keys/KEYS_1_1
- C4 pad 1: /multiplexers/keys/KEYS_0_1 -> +3V3
- C40 pad 1: /multiplexers/keys/KEYS_1_5 -> /multiplexers/keys/KEYS_1_2
- C42 pad 1: /multiplexers/keys/KEYS_1_6 -> /multiplexers/keys/KEYS_1_3
- C44 pad 1: /multiplexers/keys/KEYS_1_7 -> /multiplexers/keys/KEYS_1_4
- C46 pad 1: /multiplexers/keys/KEYS_1_8 -> /multiplexers/keys/KEYS_1_5
- C48 pad 1: /multiplexers/keys/KEYS_1_9 -> /multiplexers/keys/KEYS_1_6
- C5 pad 1: GND -> +3V3
- C5 pad 2: +3V3 -> GND
- C50 pad 1: /multiplexers/keys/KEYS_1_10 -> /multiplexers/keys/KEYS_1_7
- C52 pad 1: /multiplexers/keys/KEYS_1_11 -> /multiplexers/keys/KEYS_1_8
- C54 pad 1: /multiplexers/keys/KEYS_1_12 -> /multiplexers/keys/KEYS_1_9
- C56 pad 1: /multiplexers/keys/KEYS_1_13 -> /multiplexers/keys/KEYS_1_10
- C58 pad 1: /multiplexers/keys/KEYS_1_14 -> /multiplexers/keys/KEYS_1_11
- C6 pad 1: /multiplexers/keys/KEYS_0_2 -> +3V3
- C60 pad 1: /multiplexers/keys/KEYS_1_15 -> /multiplexers/keys/KEYS_1_12
- C62 pad 1: /multiplexers/keys/KEYS_2_0 -> /multiplexers/keys/KEYS_1_13
- C64 pad 1: /multiplexers/keys/KEYS_2_1 -> /multiplexers/keys/KEYS_1_14
- C66 pad 1: /multiplexers/keys/KEYS_2_2 -> /multiplexers/keys/KEYS_2_0
- C68 pad 1: /multiplexers/keys/KEYS_2_3 -> /multiplexers/keys/KEYS_2_1
- C70 pad 1: /multiplexers/keys/KEYS_2_4 -> /multiplexers/keys/KEYS_2_2
- C72 pad 1: /multiplexers/keys/KEYS_2_5 -> /multiplexers/keys/KEYS_2_3
- C74 pad 1: /multiplexers/keys/KEYS_2_6 -> /multiplexers/keys/KEYS_2_4
- C76 pad 1: /multiplexers/keys/KEYS_2_7 -> /multiplexers/keys/KEYS_2_5
- C78 pad 1: /multiplexers/keys/KEYS_2_8 -> /multiplexers/keys/KEYS_2_6
- C8 pad 1: /multiplexers/keys/KEYS_0_3 -> /multiplexers/keys/KEYS_0_0
- C80 pad 1: /multiplexers/keys/KEYS_2_9 -> /multiplexers/keys/KEYS_2_7
- C82 pad 1: /multiplexers/keys/KEYS_2_10 -> /multiplexers/keys/KEYS_2_8
- C84 pad 1: /multiplexers/keys/KEYS_2_11 -> /multiplexers/keys/KEYS_2_9
- C86 pad 1: /multiplexers/keys/KEYS_2_12 -> /multiplexers/keys/KEYS_2_10
- C88 pad 1: /multiplexers/keys/KEYS_2_13 -> /multiplexers/keys/KEYS_2_11
- C90 pad 1: /multiplexers/keys/KEYS_2_14 -> /multiplexers/keys/KEYS_2_12
- C92 pad 1: /multiplexers/keys/KEYS_2_15 -> /multiplexers/keys/KEYS_2_13
- C94 pad 1: /multiplexers/keys/KEYS_3_0 -> /multiplexers/keys/KEYS_2_14
- C96 pad 1: /multiplexers/keys/KEYS_3_1 -> /multiplexers/keys/KEYS_3_0
- C98 pad 1: /multiplexers/keys/KEYS_3_2 -> /multiplexers/keys/KEYS_3_1
- R30 pad 1: /multiplexers/keys/KEYS_1_15 -> /multiplexers/keys/KEYS_2_0
- R31 pad 1: /multiplexers/keys/KEYS_2_0 -> /multiplexers/keys/KEYS_2_1
- R32 pad 1: /multiplexers/keys/KEYS_2_1 -> /multiplexers/keys/KEYS_2_2
- R33 pad 1: /multiplexers/keys/KEYS_2_2 -> /multiplexers/keys/KEYS_2_3
- R34 pad 1: /multiplexers/keys/KEYS_2_3 -> /multiplexers/keys/KEYS_2_4
- R35 pad 1: /multiplexers/keys/KEYS_2_4 -> /multiplexers/keys/KEYS_2_5
- R36 pad 1: /multiplexers/keys/KEYS_2_5 -> /multiplexers/keys/KEYS_2_6
- R37 pad 1: /multiplexers/keys/KEYS_2_6 -> /multiplexers/keys/KEYS_2_7
- R38 pad 1: /multiplexers/keys/KEYS_2_7 -> /multiplexers/keys/KEYS_2_8
- R39 pad 1: /multiplexers/keys/KEYS_2_8 -> /multiplexers/keys/KEYS_2_9
- R40 pad 1: /multiplexers/keys/KEYS_2_9 -> /multiplexers/keys/KEYS_2_10
- R41 pad 1: /multiplexers/keys/KEYS_2_10 -> /multiplexers/keys/KEYS_2_11
- R42 pad 1: /multiplexers/keys/KEYS_2_11 -> /multiplexers/keys/KEYS_2_12
- R43 pad 1: /multiplexers/keys/KEYS_2_12 -> /multiplexers/keys/KEYS_2_13
- R44 pad 1: /multiplexers/keys/KEYS_2_13 -> /multiplexers/keys/KEYS_2_14
- R45 pad 1: /multiplexers/keys/KEYS_2_14 -> /multiplexers/keys/KEYS_3_0
- R46 pad 1: /multiplexers/keys/KEYS_2_15 -> /multiplexers/keys/KEYS_3_1
- R47 pad 1: /multiplexers/keys/KEYS_3_0 -> /multiplexers/keys/KEYS_3_2
- R48 pad 1: /multiplexers/keys/KEYS_3_1 -> /multiplexers/keys/KEYS_3_3
- R49 pad 1: /multiplexers/keys/KEYS_3_2 -> /multiplexers/keys/KEYS_3_4
- R50 pad 1: /multiplexers/keys/KEYS_3_3 -> /multiplexers/keys/KEYS_3_5
- R51 pad 1: /multiplexers/keys/KEYS_3_4 -> /multiplexers/keys/KEYS_3_6
- R52 pad 1: /multiplexers/keys/KEYS_3_5 -> /multiplexers/keys/KEYS_3_7
- R53 pad 1: /multiplexers/keys/KEYS_3_6 -> /multiplexers/keys/KEYS_3_8
- R54 pad 1: /multiplexers/keys/KEYS_3_7 -> /multiplexers/keys/KEYS_3_9
- R55 pad 1: /multiplexers/keys/KEYS_3_8 -> /multiplexers/keys/KEYS_3_10
- R56 pad 1: /multiplexers/keys/KEYS_3_9 -> /multiplexers/keys/KEYS_3_11
- R57 pad 1: /multiplexers/keys/KEYS_3_10 -> /multiplexers/keys/KEYS_3_12
- R58 pad 1: /multiplexers/keys/KEYS_3_11 -> /multiplexers/keys/KEYS_3_13
- R59 pad 1: /multiplexers/keys/KEYS_3_12 -> /multiplexers/keys/KEYS_4_0
- R60 pad 1: /multiplexers/keys/KEYS_3_13 -> /multiplexers/keys/KEYS_4_1
- R61 pad 1: /multiplexers/keys/KEYS_4_0 -> /multiplexers/keys/KEYS_4_2
- R62 pad 1: /multiplexers/keys/KEYS_4_1 -> /multiplexers/keys/KEYS_4_3
- R63 pad 1: /multiplexers/keys/KEYS_4_2 -> /multiplexers/keys/KEYS_4_4
- R64 pad 1: /multiplexers/keys/KEYS_4_3 -> /multiplexers/keys/KEYS_4_5
- R65 pad 1: /multiplexers/keys/KEYS_4_4 -> /multiplexers/keys/KEYS_4_7
- R66 pad 1: /multiplexers/keys/KEYS_4_5 -> /multiplexers/keys/KEYS_4_8
- R67 pad 1: /multiplexers/keys/KEYS_4_6 -> /multiplexers/keys/KEYS_4_9
- R68 pad 1: /multiplexers/keys/KEYS_4_7 -> /multiplexers/keys/KEYS_4_10
- R69 pad 1: /multiplexers/keys/KEYS_4_8 -> /multiplexers/keys/KEYS_4_11
- R70 pad 1: /multiplexers/keys/KEYS_4_9 -> /multiplexers/keys/KEYS_4_12
- R71 pad 1: /multiplexers/keys/KEYS_4_10 -> /multiplexers/keys/KEYS_4_13
- R72 pad 1: /multiplexers/keys/KEYS_4_11 -> /multiplexers/keys/KEYS_5_0
- R73 pad 1: /multiplexers/keys/KEYS_4_12 -> /multiplexers/keys/KEYS_5_1
- R74 pad 1: /multiplexers/keys/KEYS_5_0 -> /multiplexers/keys/KEYS_5_2
- R75 pad 1: /multiplexers/keys/KEYS_5_1 -> /multiplexers/keys/KEYS_5_3
- R76 pad 1: /multiplexers/keys/KEYS_5_2 -> /multiplexers/keys/KEYS_5_4
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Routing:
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
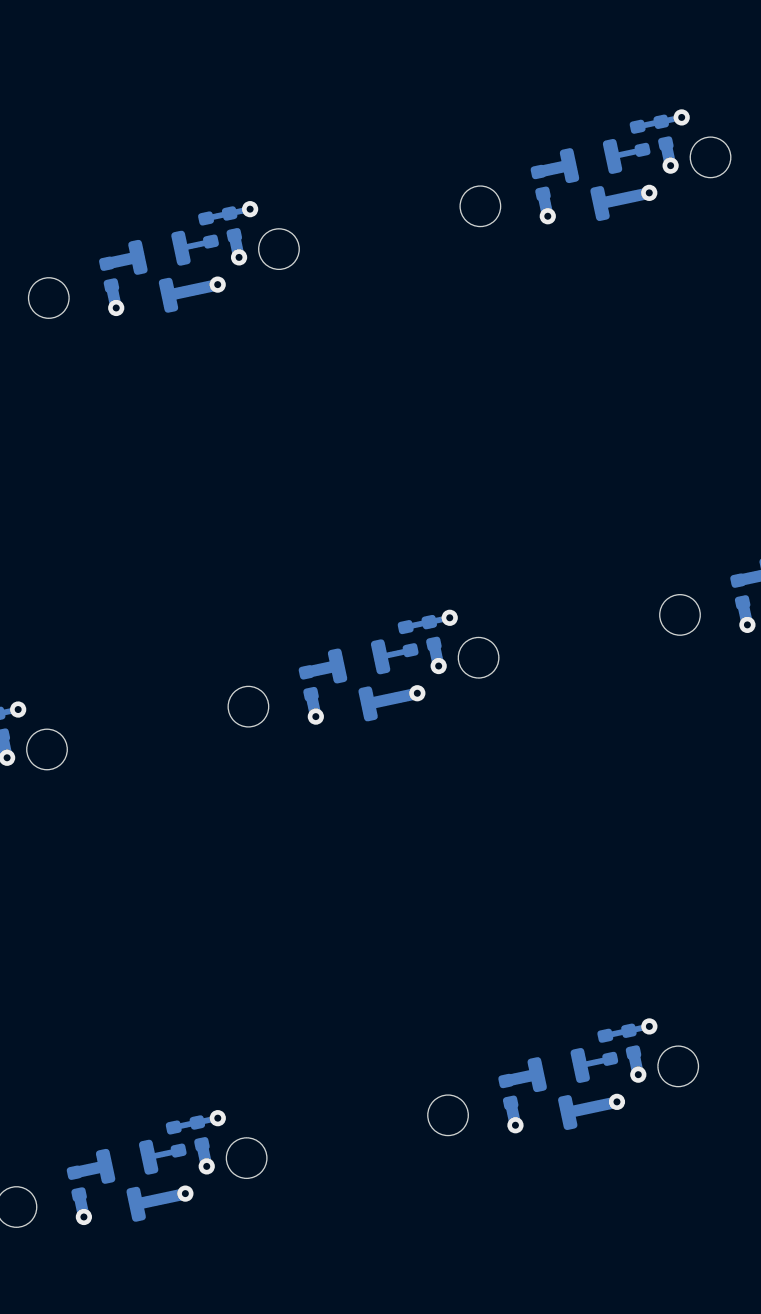
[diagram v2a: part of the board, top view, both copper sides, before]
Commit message: Migrating to AT32F415CBT7
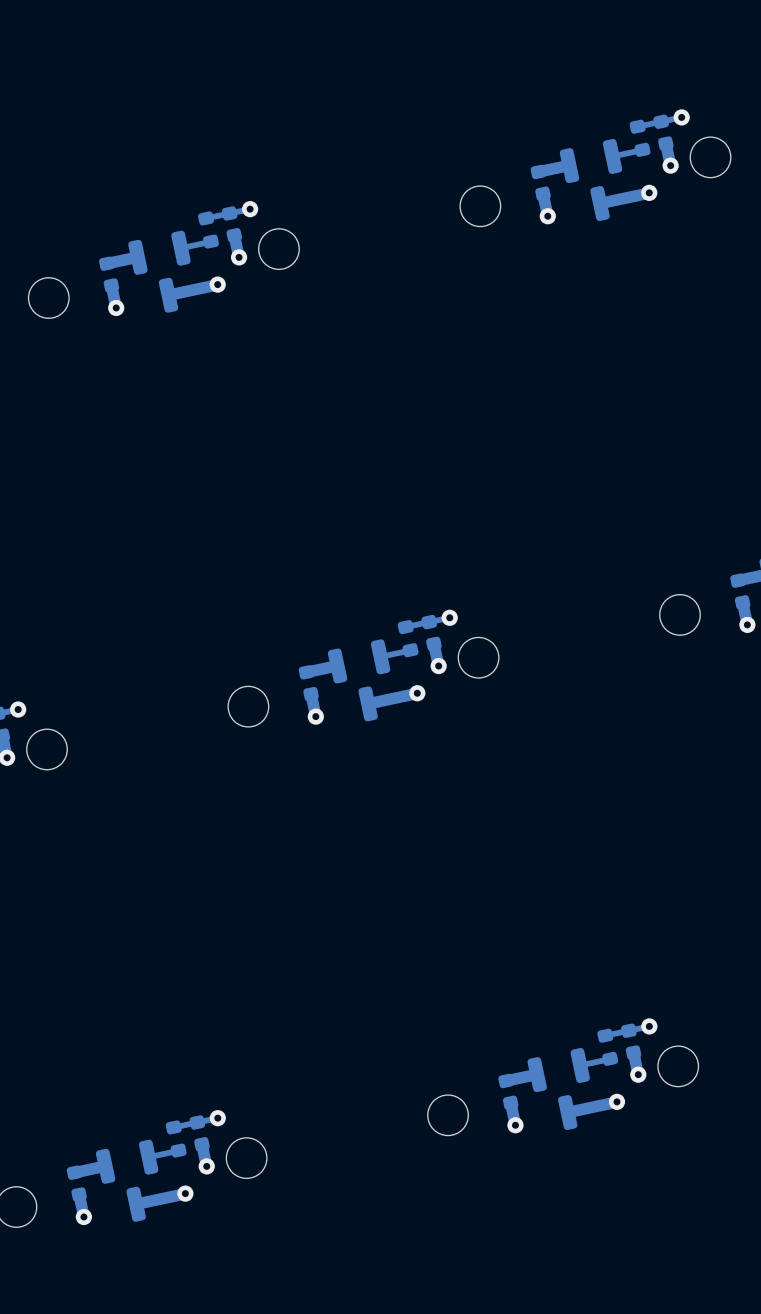
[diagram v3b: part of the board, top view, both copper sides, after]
